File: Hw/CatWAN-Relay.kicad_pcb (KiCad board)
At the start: 2 copper layers, 50 x 86.9 mm, 56 parts, among them J2 INPUTS, J3 OUTPUTS, J4 I2C, J5 Serial, P1 USB_C_Plug_USB2.0, Q1 MMBT2222A, Q2 MMBT2222A, Q3 MMBT2222A, SW1 BOOT, SW2 RESET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

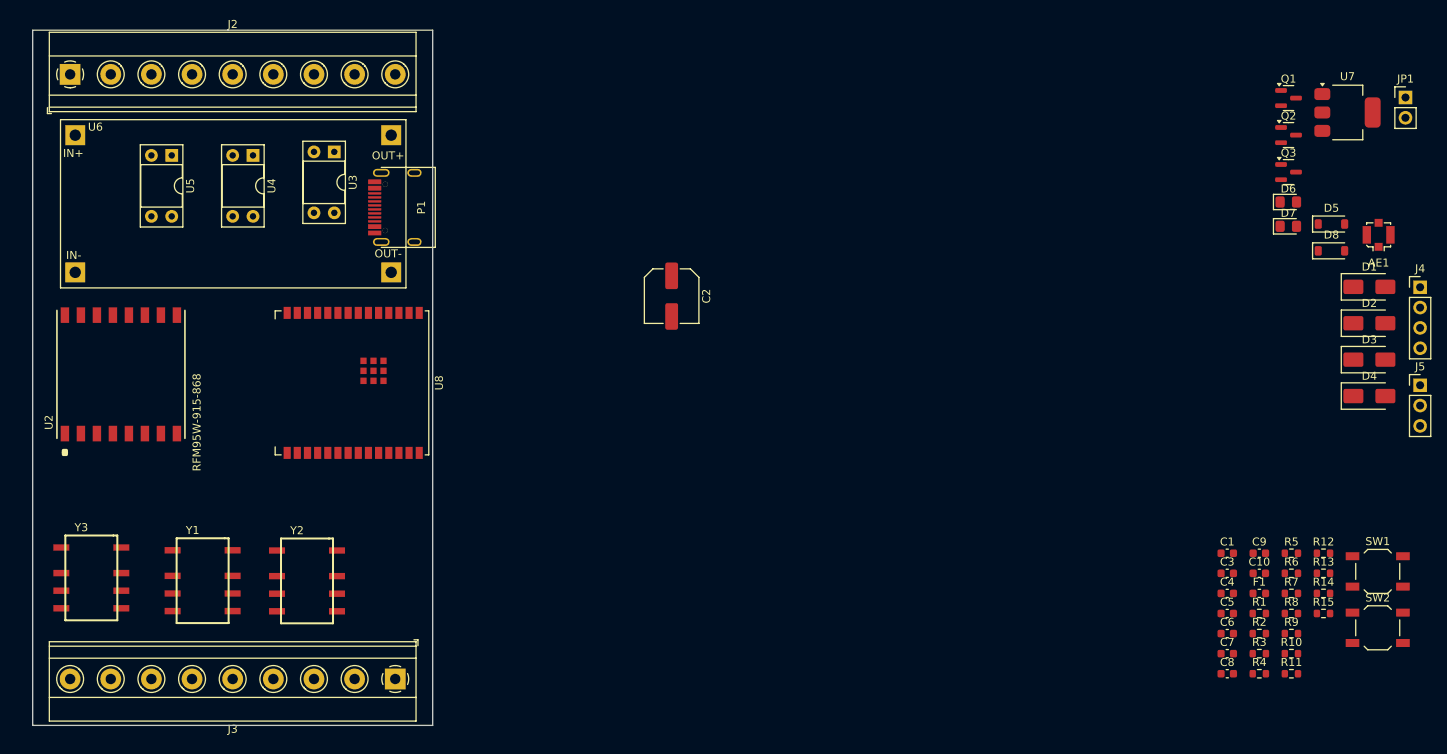
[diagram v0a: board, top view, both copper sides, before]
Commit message: feat(hw): Change optocoupler and D1-D4 mfr# and update footprints
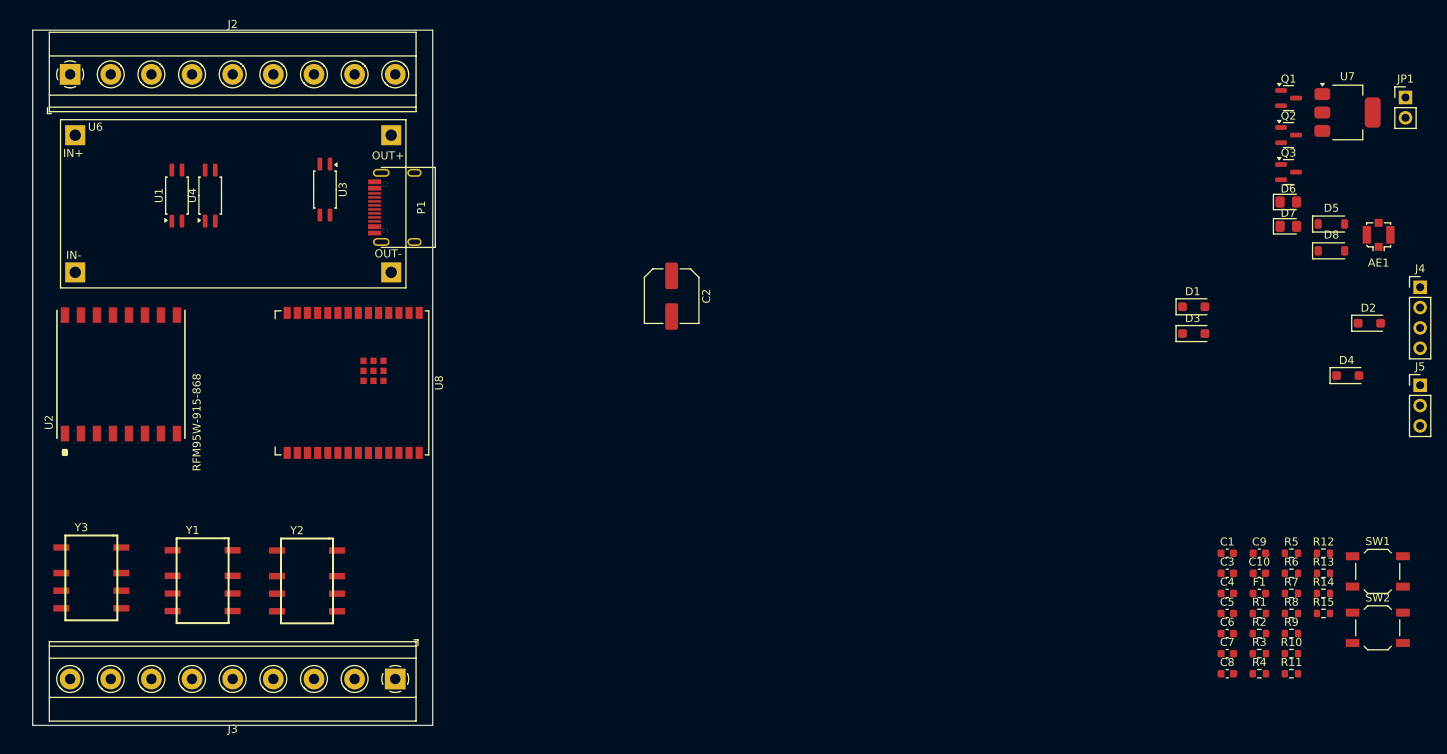
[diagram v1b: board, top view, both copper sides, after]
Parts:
- removed U5: LTV-817, Package_DIP:DIP-4_W7.62mm_Socket
- added U1: AT3H7C-CuH-S, Package_SO:SOP-4_4.4x2.6mm_P1.27mm, F.Cu at (59.5, 58.2)
- D1, D2, D3, D4: value RS1M -> SOD4007-MS; footprint Diode_SMD:D_SMA -> Diode_SMD:D_SOD-123F
- U3, U4: value LTV-817 -> AT3H7C-CuH-S; footprint Package_DIP:DIP-4_W7.62mm_Socket -> Package_SO:SOP-4_4.4x2.6mm_P1.27mm
- moved D3 22.2 mm to (186.6, 75.5)
- moved D1 22.1 mm to (186.6, 72.2)
- moved U4 7.34 mm to (63.7, 58.2), turned to 90 degrees
- moved U3 4.85 mm to (78.0, 57.5)
- moved D4 3.72 mm to (205.8, 80.8)
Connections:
- U3 pad 1: Net-(R3-Pad1) -> Net-(R6-Pad1)
- U3 pad 2: /IA2 -> /IB2
- U3 pad 4: /DI3 -> /DI2
- U4 pad 1: Net-(R6-Pad1) -> Net-(R8-Pad1)
- U4 pad 2: /IB2 -> /IC2
- U4 pad 4: /DI2 -> /DI1

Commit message: feat: components placed
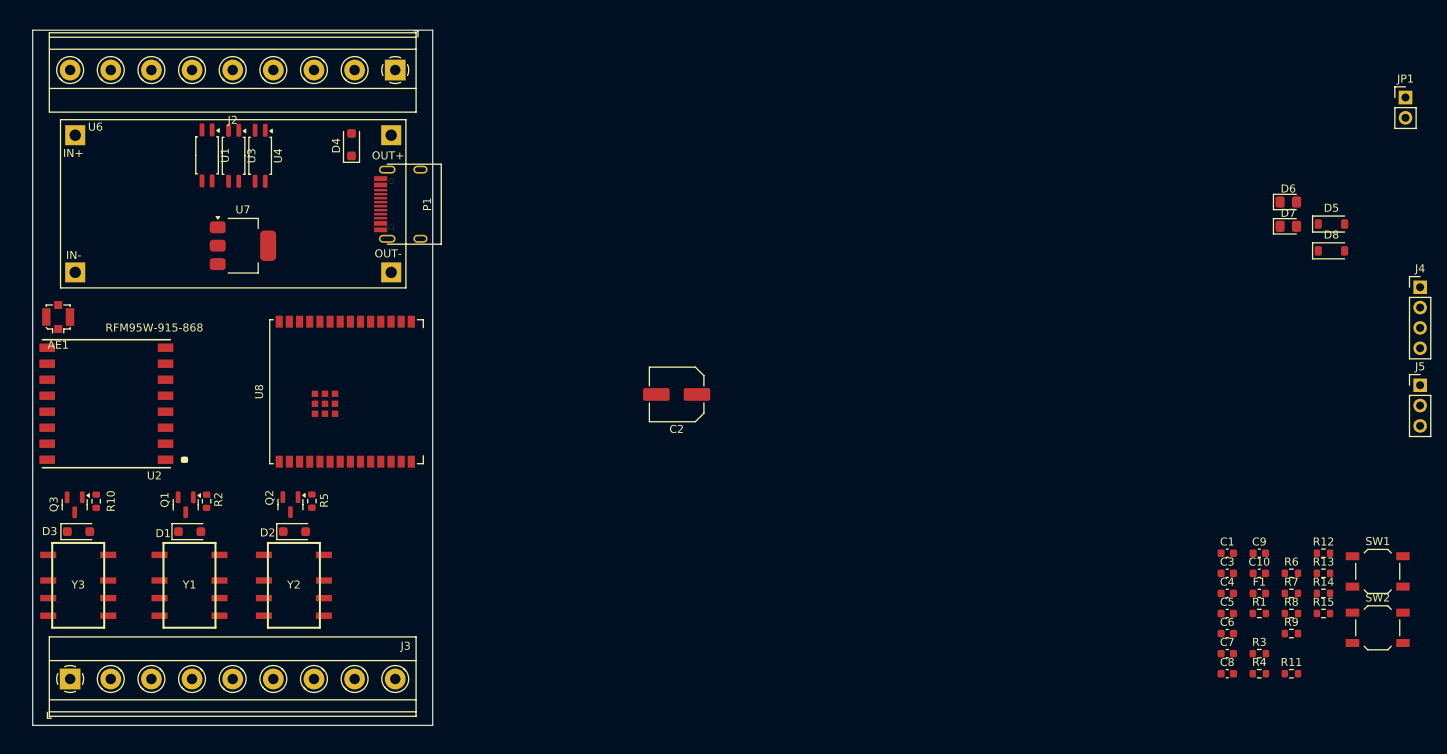
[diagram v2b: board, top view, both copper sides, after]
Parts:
- moved AE1 165.4 mm to (44.7, 73.4)
- moved Q3 157.3 mm to (46.7, 96.9), turned to -90 degrees
- moved R10 150.6 mm to (49.4, 96.5), turned to 90 degrees
- moved Q1 146.9 mm to (60.6, 96.9), turned to -90 degrees
- moved D3 141.6 mm to (47.2, 100.3)
- moved U7 139.1 mm to (67.8, 64.5)
- moved D2 136.9 mm to (74.2, 100.3)
- moved Q2 133.0 mm to (73.7, 96.9), turned to -90 degrees
- moved R2 132.6 mm to (63.2, 96.5), turned to 90 degrees
- moved D1 128.6 mm to (61.1, 100.3)
- moved D4 127.8 mm to (81.3, 51.9), turned to 90 degrees
- moved R5 122.6 mm to (76.4, 96.4), turned to 90 degrees
- moved J2 40.6 mm to (86.8, 42.6), turned to 180 degrees
- moved J3 40.6 mm to (46.1, 118.7), turned to 0 degrees
- moved C2 12.3 mm to (122.0, 83.1), turned to 180 degrees
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
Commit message: feat: Boot and Reset buttons footprint changed
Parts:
- SW1, SW2: footprint Button_Switch_SMD:SW_SPST_TL3342 -> Button_Switch_SMD:SW_Push_SPST_NO_Alps_SKRK

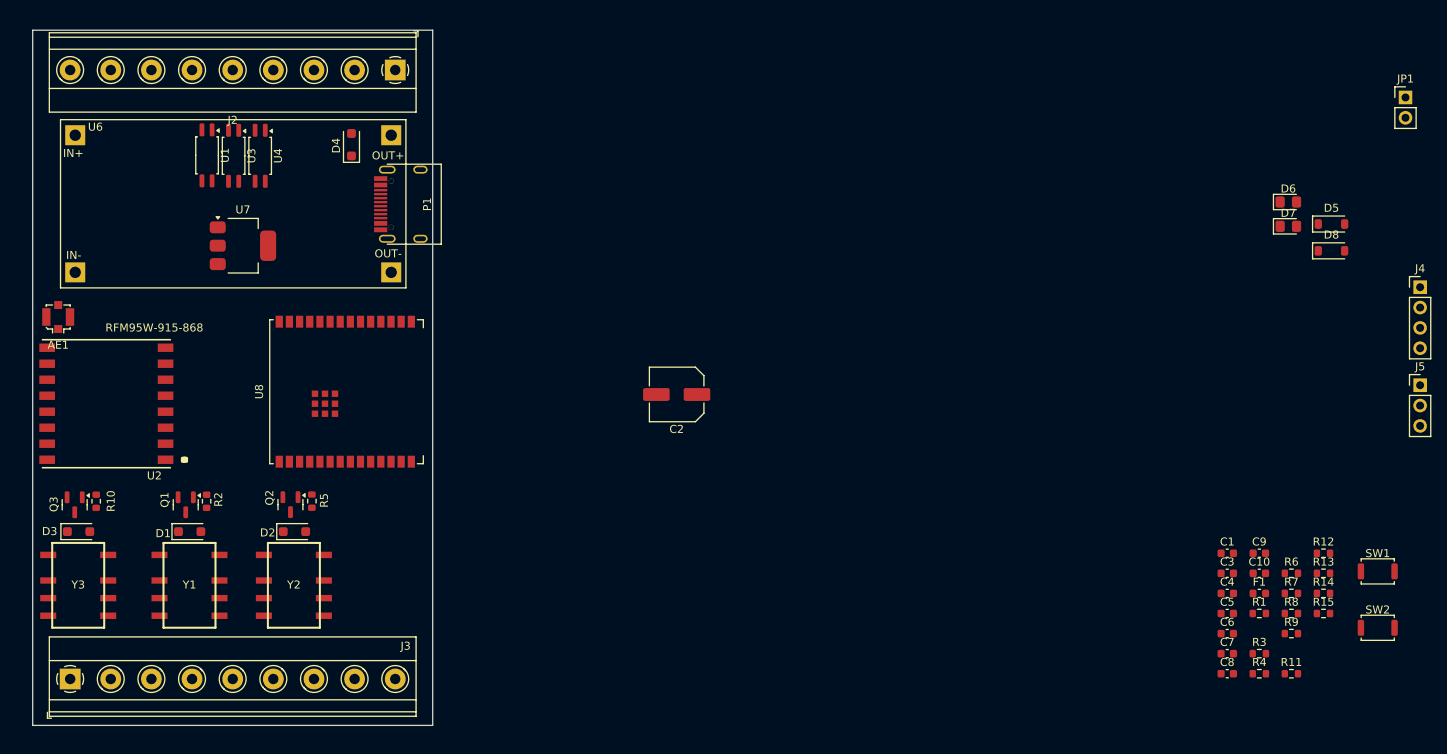
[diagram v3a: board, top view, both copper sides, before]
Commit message: Feat: floorplan added
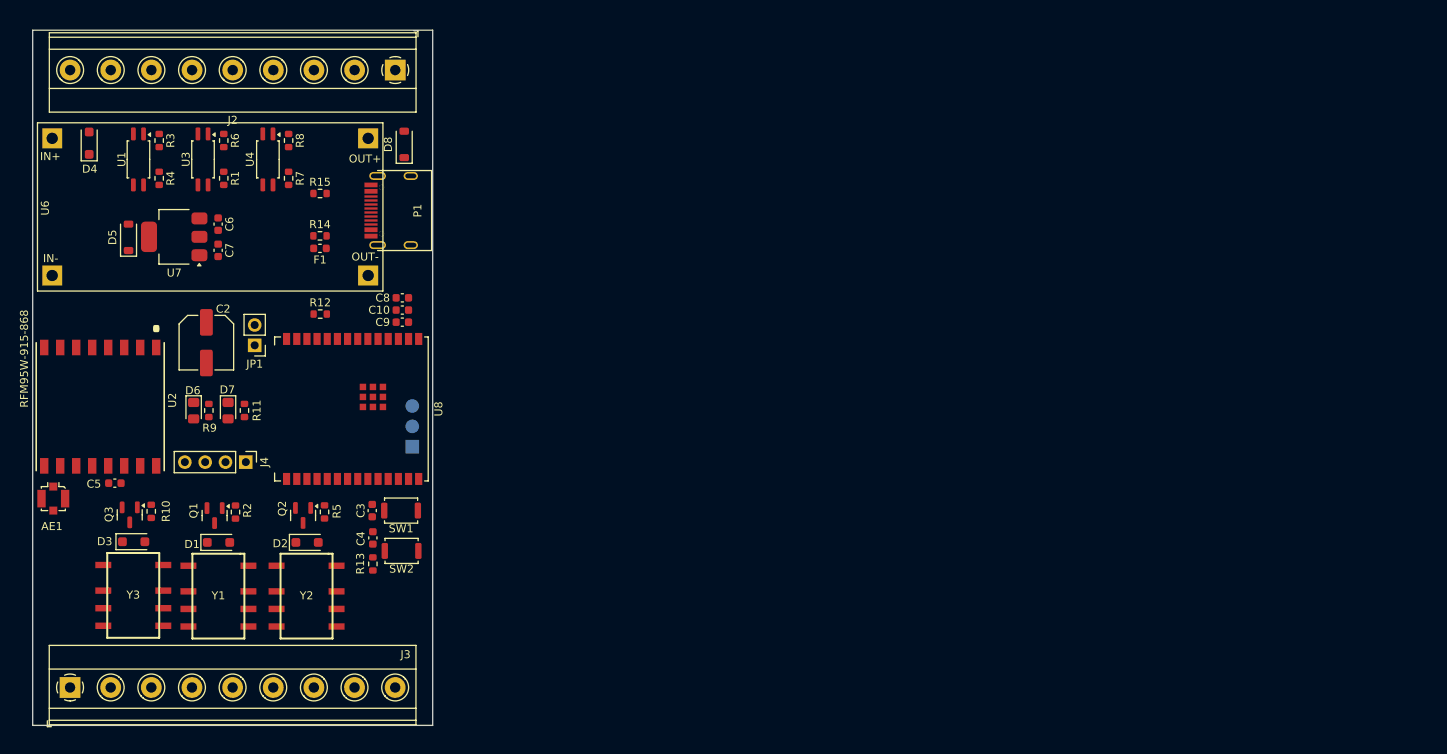
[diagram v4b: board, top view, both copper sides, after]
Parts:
- removed C1: 0.1uF, Capacitor_SMD:C_0603_1608Metric
- J5: moved to B.Cu
- moved R3 151.7 mm to (57.3, 51.4), turned to -90 degrees
- moved R4 150.8 mm to (57.3, 56.1), turned to -90 degrees
- moved D5 150.4 mm to (53.5, 63.5), turned to 90 degrees
- moved J4 148.4 mm to (68.1, 91.6), turned to -90 degrees
- moved JP1 147.1 mm to (69.2, 77.0), turned to 180 degrees
- moved R6 144.0 mm to (65.3, 51.4), turned to -90 degrees
- moved R1 140.4 mm to (65.3, 56.1), turned to -90 degrees
- moved C5 140.0 mm to (51.7, 94.2)
- moved D6 139.3 mm to (61.6, 85.1), turned to -90 degrees
- moved R8 138.6 mm to (73.5, 51.4), turned to -90 degrees
- moved R9 138.2 mm to (63.5, 85.1), turned to -90 degrees
- moved C6 136.1 mm to (64.7, 61.8), turned to -90 degrees
- moved R15 136.0 mm to (77.4, 58.0)
- moved C7 135.8 mm to (64.7, 65.1), turned to -90 degrees
- moved R7 135.7 mm to (73.5, 56.1), turned to -90 degrees
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
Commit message: feat(Hw):First_Route_v2
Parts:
- moved Y3 25.9 mm to (76.7, 101.7)
- moved R10 25.9 mm to (82.2, 96.5)
- moved D3 25.9 mm to (80.0, 100.3)
- moved Q3 25.9 mm to (79.5, 97.2)
- moved D8 22.5 mm to (73.4, 69.1), turned to 180 degrees
- moved Q1 15.8 mm to (48.5, 96.9)
- moved D1 15.2 mm to (49.5, 100.3)
- moved Y1 15.2 mm to (46.2, 101.7)
- moved R2 15.2 mm to (51.6, 96.5)
- moved Y2 10.3 mm to (62.3, 101.7)
- moved D2 10.3 mm to (65.6, 100.3)
- moved Q2 10.3 mm to (65.1, 97.0)
- moved R5 10.3 mm to (67.8, 96.5)
- moved F1 8.67 mm to (80.5, 56.8)
- moved C4 6.75 mm to (89.8, 104.5), turned to 180 degrees
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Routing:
- net +3V3: track 0.00 -> 240.2 mm, vias 0 -> 10
- net /DIO5: track 0.00 -> 61.0 mm, vias 0 -> 2
- net /DI2: track 0.00 -> 56.7 mm, vias 0 -> 2
- net /RFM_RST: track 0.00 -> 56.1 mm, vias 0 -> 2
- net /DO3: track 0.00 -> 52.0 mm, vias 0 -> 2
- net /DIO2: track 0.00 -> 50.1 mm, vias 0 -> 2
- net /SCK: track 0.00 -> 49.3 mm
- net /DI3: track 0.00 -> 45.1 mm, vias 0 -> 2
- net /SS: track 0.00 -> 45.1 mm, vias 0 -> 2
- net /MOSI: track 0.00 -> 42.2 mm
- net /DO1: track 0.00 -> 41.9 mm, vias 0 -> 2
- net /MISO: track 0.00 -> 41.4 mm
- net /EN: track 0.00 -> 38.7 mm, vias 0 -> 2
- net /DIO0: track 0.00 -> 37.2 mm, vias 0 -> 2
- net /DIO1: track 0.00 -> 36.3 mm, vias 0 -> 2
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- added copper zone on B.Cu, net GND
- added copper zone on F.Cu, net GND

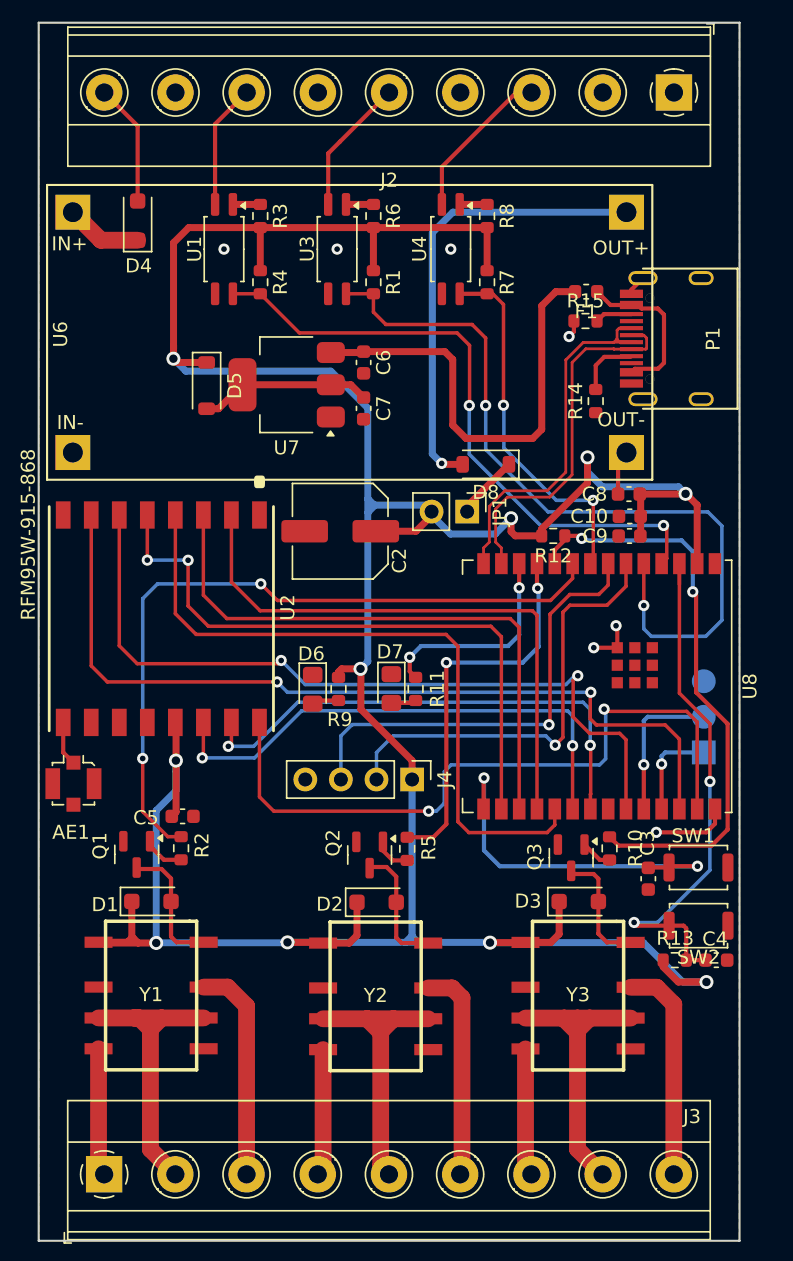
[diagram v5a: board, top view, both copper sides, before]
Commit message: feat: add zone with no fill
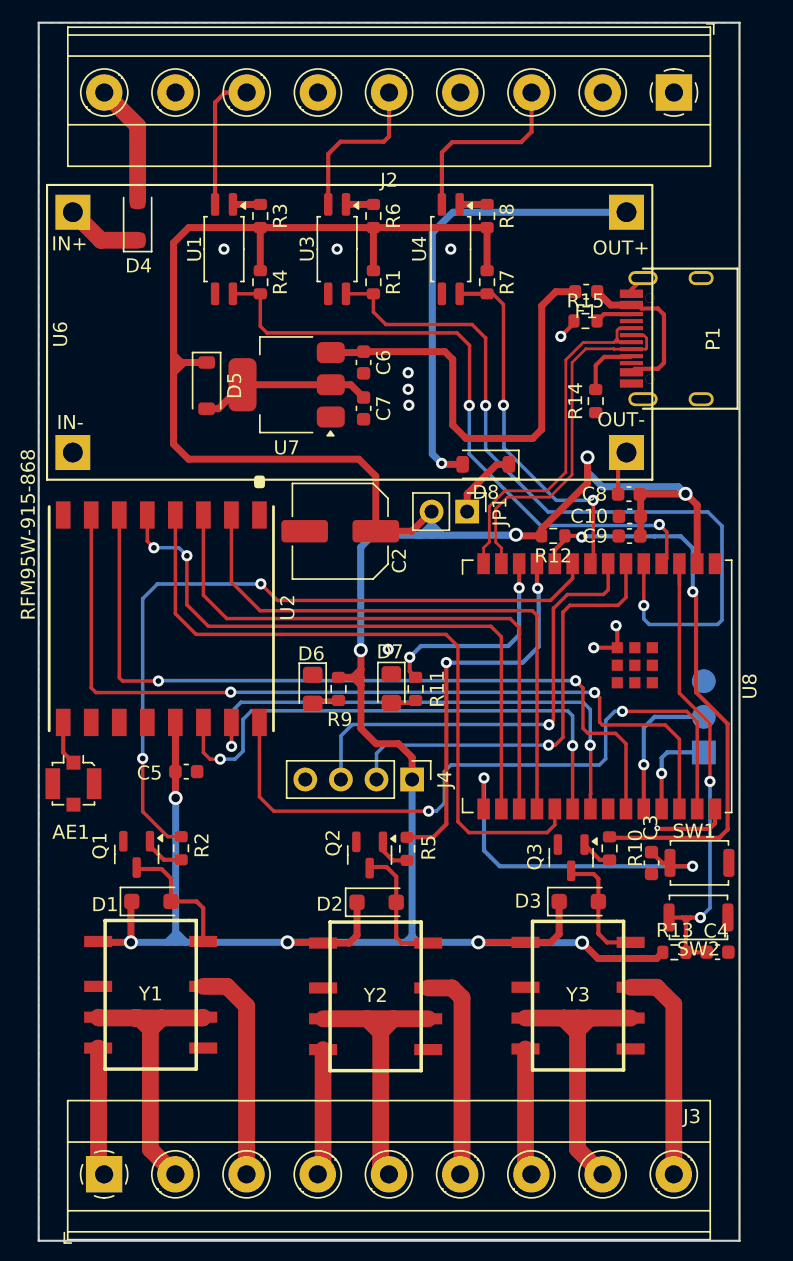
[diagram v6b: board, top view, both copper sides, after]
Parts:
- moved C5 3.20 mm to (52.0, 91.0)
- moved C3 1.14 mm to (85.2, 97.5)
- moved SW2 0.59 mm to (88.5, 101.4)
- moved C4 0.58 mm to (89.9, 103.9)
- moved R13 0.56 mm to (86.8, 103.9)
- moved SW1 0.34 mm to (88.6, 97.5)
- moved Y1 0.06 mm to (46.2, 101.6)
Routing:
- net +3V3: track 240.2 -> 233.0 mm, vias 10 -> 9
- net /EN: track 38.7 -> 35.0 mm
- net /IC2: track 11.3 -> 13.5 mm
- net /IB2: track 9.78 -> 11.6 mm
- net /DI3: track 45.1 -> 46.4 mm
- net /DIO1: track 36.3 -> 37.4 mm
- net /DI2: track 56.7 -> 55.6 mm
- net /DIO0: track 37.2 -> 38.2 mm
- net /IA2: track 8.92 -> 9.82 mm
- net /DIO5: track 61.0 -> 61.8 mm
- net /DIO2: track 50.1 -> 49.4 mm
- net /SS: track 45.1 -> 44.4 mm
- net /BOOT: track 26.7 -> 26.1 mm
- net Net-(D8-K): track 4.60 -> 5.11 mm
- net GND: track 14.7 -> 14.8 mm, vias 7 -> 11
